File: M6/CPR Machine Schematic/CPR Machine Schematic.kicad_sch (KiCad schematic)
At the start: 0 parts

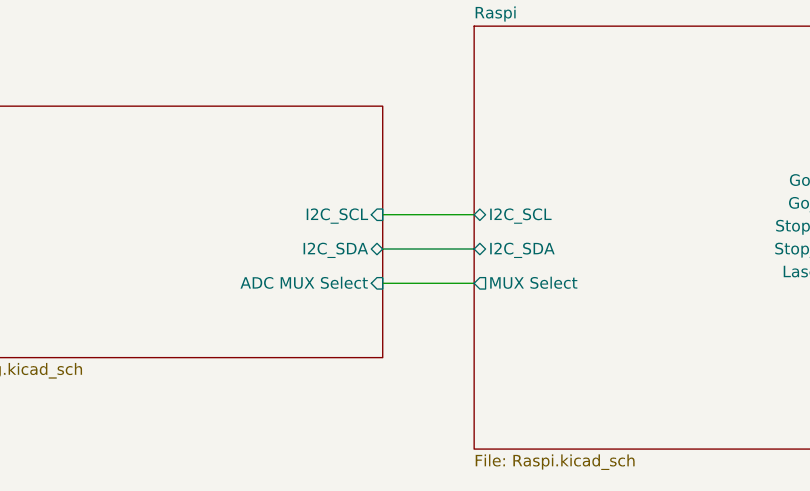
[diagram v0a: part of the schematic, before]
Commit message: Updated ADC Logic Level, Redone Layout, Geographic Reannotation
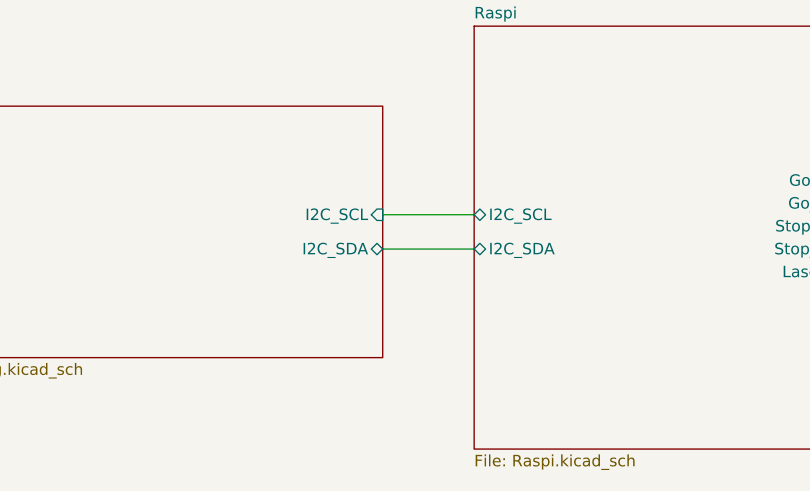
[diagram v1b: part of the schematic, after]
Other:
- sheet Raspi ports: added none; removed MUX Select
- sheet Sensing ports: added none; removed ADC MUX Select
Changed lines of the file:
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@@
-		)
-	)
-	(wire
-		(pts
-			(xy 110.49 87.63) (xy 120.65 87.63)
-		)
-		(stroke
-			(width 0)
-			(type default)
 		)
 	)
@@
 		(pin "I2C_SDA" bidirectional
 			(at 110.49 83.82 0)
-			(effects
-				(font
-					(size 1.27 1.27)
-				)
-				(justify right)
-			)
-		)
-		(pin "ADC MUX Select" input
-			(at 110.49 87.63 0)
 			(effects
 				(font
@@
 			)
 		)
-		(pin "MUX Select" output
-			(at 120.65 87.63 180)
-			(effects
-				(font
-					(size 1.27 1.27)
-				)
-				(justify left)
-			)
-		)
